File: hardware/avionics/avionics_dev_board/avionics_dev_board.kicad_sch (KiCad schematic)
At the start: 13 parts, among them J1 Screw_Term_1x2, SW1 SW_Push, U1 TPS563200

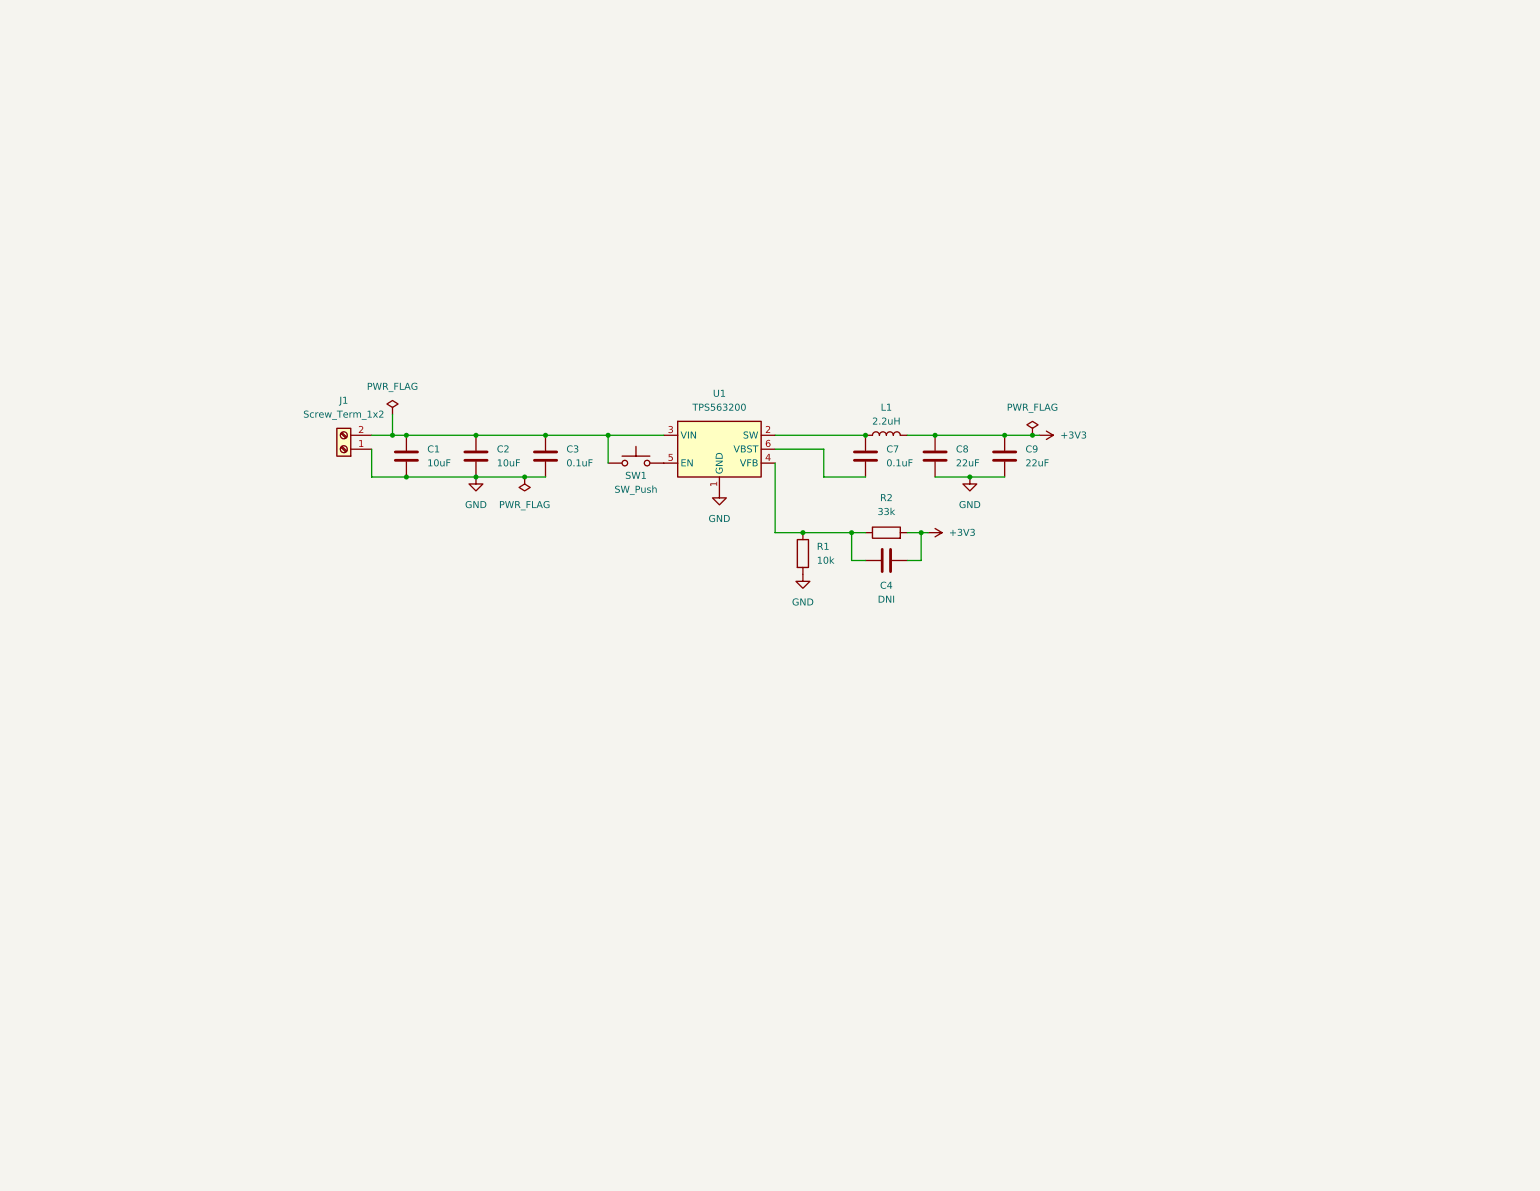
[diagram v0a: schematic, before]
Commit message: Fixed packet sequence miscouting error and finalised avionics component selections
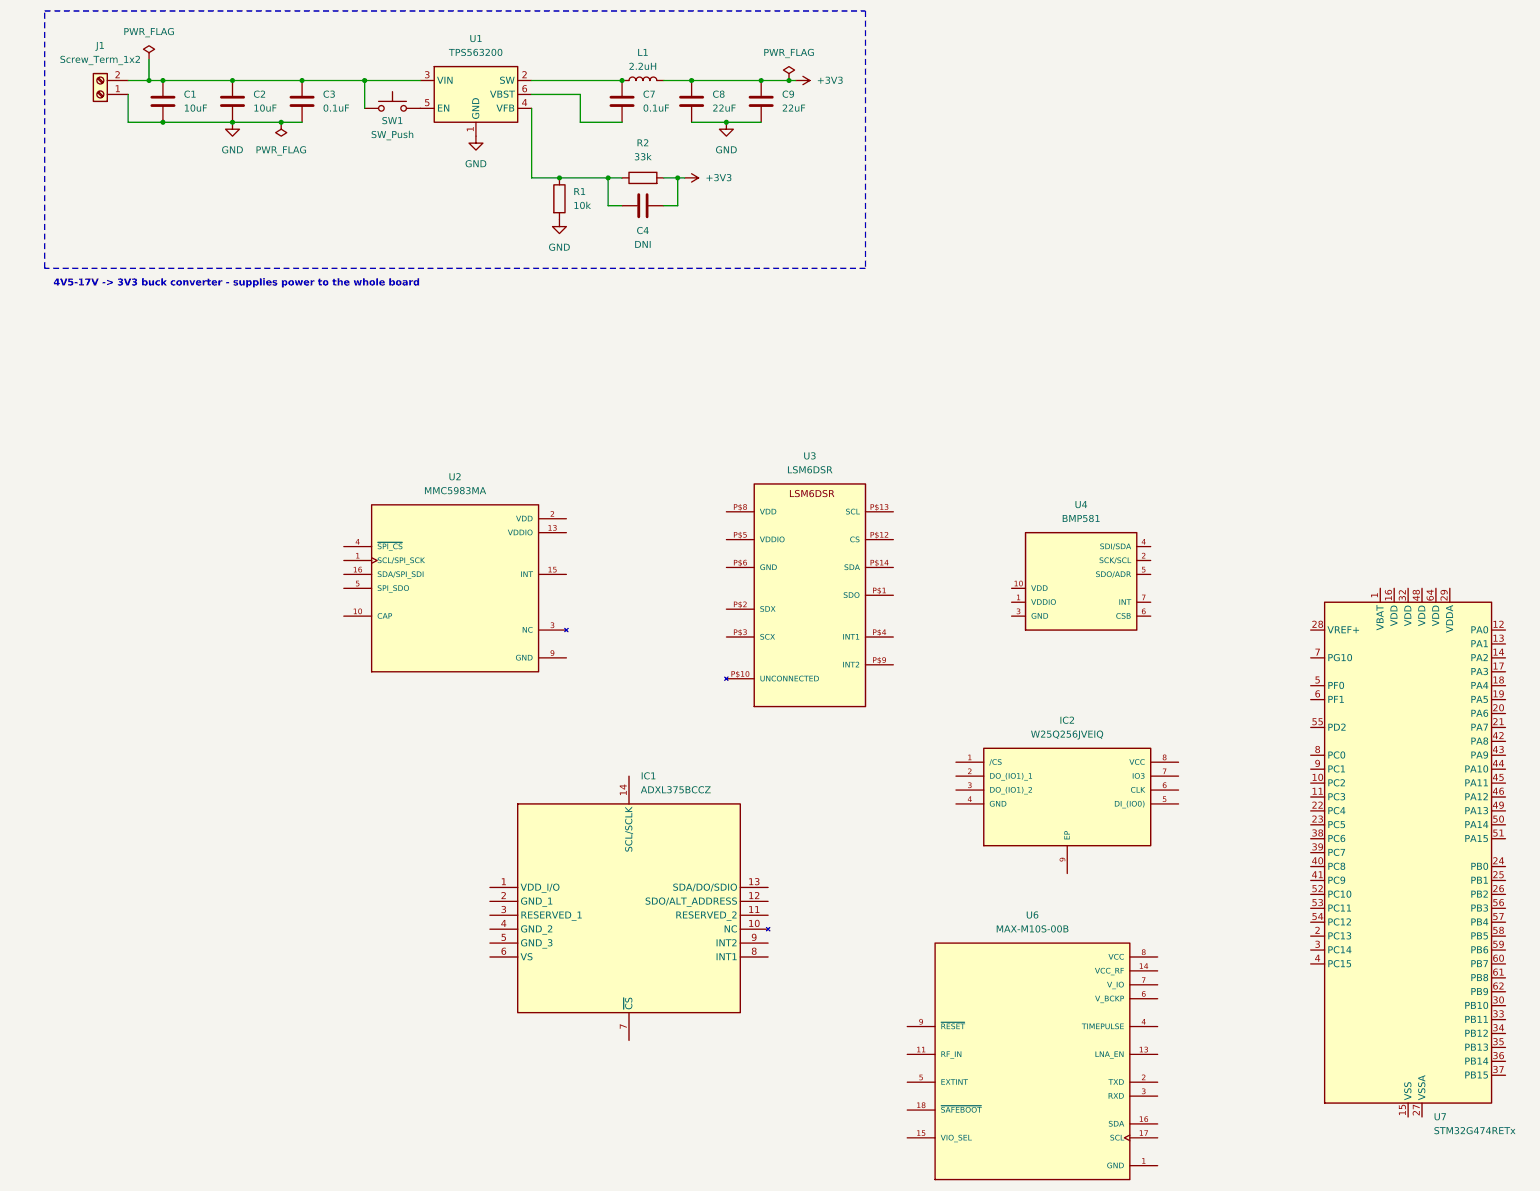
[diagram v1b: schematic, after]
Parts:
- added IC1: ADXL375BCCZ, CC-14-1, symbol ADXL375BCCZ:ADXL375BCCZ
- added IC2: W25Q256JVEIQ, W25Q256JVEIQ:SON127P800X600X80-9N, symbol W25Q256JVEIQ:W25Q256JVEIQ
- added U2: MMC5983MA, MMC5983MA:PQFN50P300X300X100-16N, symbol MMC5983MA:MMC5983MA
- added U3: LSM6DSR, LSM6DSR:LGA-14L, symbol LSM6DSR:LSM6DSR
- added U4: BMP581, BMP581:BMP581, symbol BMP581:BMP581
- added U6: MAX-M10S-00B, MAX-M10S-00B:XCVR_MAX-M10S-00B, symbol MAX-M10S-00B:MAX-M10S-00B
- added U7: STM32G474RETx, Package_QFP:LQFP-64_10x10mm_P0.5mm, symbol MCU_ST_STM32G4:STM32G474RETx
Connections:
- net GND: now also U2.11 (GND), U2.9 (GND), U3.P$6 (GND), U3.P$7 (GND), U4.3 (GND), U4.8 (GND), U4.9 (GND), U6.1 (GND), U6.10 (GND), U6.12 (GND)
- new net: U2.12 (NC), U2.14 (NC), U2.3 (NC), U2.6 (NC), U2.7 (NC), U2.8 (NC)
- new net: U3.P$10 (UNCONNECTED), U3.P$11 (UNCONNECTED)
- new net: U7.15 (VSS), U7.31 (VSS), U7.47 (VSS), U7.63 (VSS)
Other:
- note added: "4V5-17V -> 3V3 buck converter - supplies power to the whole board"
- moved on the sheet: C1, C2, C3, C4, C7, C8, C9, J1, L1, R1, R2, SW1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

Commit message: Started designing stm32g474ret6 section of the PCB schematic. Done power supply, external crystal oscillator, and BOOT0 and NRST pins so far
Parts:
- added C10, C11, C12, C15, C17, C19, C22, C5: 100nF, symbol Device:C
- added C13, C16, C18: 1uF, symbol Device:C
- added C14: 10nF, symbol Device:C
- added C20, C21: ?F, symbol Device:C
- added C6: 4u7F, symbol Device:C
- added D1: PWR LED, symbol Device:LED
- added FB1: 120R, symbol Device:FerriteBead
- added R3: 10k, Resistor_SMD:R_0603_1608Metric, symbol Device:R
- added R4: 10kR, symbol Device:R
- added SW2, SW3: SW_Push, Button_Switch_SMD:SW_DIP_SPSTx01_Slide_6.7x4.1mm_W6.73mm_P2.54mm_LowProfile_JPin, symbol Switch:SW_Push
- added Y1: 32k768Hz, symbol Device:Crystal
- C3, C7: value 0.1uF -> 0u1F
- L1: value 2.2uH -> 2u2H
- U7: value STM32G474RETx -> STM32G474RET6
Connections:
- net +3V3: now also C10.1, C11.1, C12.1, C13.1, C17.1, C5.1, C6.1, FB1.2, R3.1, SW3.2
- net GND: now also U7.1 (VBAT), U7.15 (VSS), U7.16 (VDD), U7.27 (VSSA), U7.31 (VSS), U7.32 (VDD), U7.47 (VSS), U7.48 (VDD), U7.63 (VSS), U7.64 (VDD), C10.2, C11.2, C12.2, C13.2, C14.2, C15.2, C16.2, C17.2, C18.2, C19.2, C20.2, C21.2, C22.2, C5.2, C6.2, D1.1 (K), R4.2, SW2.1
- net +3V3A: now reaches U7.28 (VREF+)
- net +3V3A: now also U7.29 (VDDA), C14.1, C15.1, C16.1, C18.1, FB1.1
- net at U7.5 (PF0): now also C20.1, Y1.1
- net at U7.6 (PF1): now also C21.1, Y1.2
- net at U7.61 (PB8): now also C22.1, R4.1, SW3.1
- net at U7.7 (PG10): now also C19.1, SW2.2
- new net: D1.2 (A), R3.2
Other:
- moved on the sheet: IC1, IC2, U2, U3, U4, U6, U7

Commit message: Updated PCB schematic with sensors and storage devices
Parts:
- added AE1: Antenna, symbol Device:Antenna
- added C23, C24, C25, C27, C28, C31, C32, C33: 100nF, symbol Device:C
- added C26, C30: 1uF, symbol Device:C
- added C29: 10uF, symbol Device:C
- added R10, R5, R6, R7, R8, R9: 2k7R, symbol Device:R
- Y1: value 32k768Hz -> 8MHz
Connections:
- net +3V3: now also IC1.1 (VDD_I/O), IC1.6 (VS), IC2.1 (/CS), IC2.8 (VCC), U2.13 (VDDIO), U2.2 (VDD), U2.4 (~{SPI_CS}), U3.P$5 (VDDIO), U3.P$8 (VDD), U4.1 (VDDIO), U4.10 (VDD), U4.6 (CSB), U6.7 (V_IO), U6.8 (VCC), C23.2, C24.2, C25.2, C26.2, C27.2, C28.2, C30.2, C31.2, C32.2, C33.2, R10.1, R5.2, R6.2, R7.2, R8.2, R9.1
- net GND: now also IC1.2 (GND_1), IC1.4 (GND_2), IC1.5 (GND_3), IC2.4 (GND), IC2.9 (EP), U3.P$2 (SDX), U3.P$3 (SCX), U4.5 (SDO/ADR), C23.1, C24.1, C25.1, C26.1, C27.1, C28.1, C29.1, C30.1, C31.1, C32.1, C33.1
- net BOOT0: now reaches C22.1, R4.1, SW3.1, U7.61 (PB8)
- net I2C2_SCL: now reaches U4.2 (SCK/SCL)
- net I2C2_SCL: now also U2.1 (SCL/SPI_SCK), U6.17 (SCL), U7.43 (PA9), R5.1, R7.1, R9.2
- net I2C2_SDA: now reaches U4.4 (SDI/SDA)
- net I2C2_SDA: now also U2.16 (SDA/SPI_SDI), U6.16 (SDA), U7.42 (PA8), R10.2, R6.1, R8.1
- net INT_BMP: now reaches U4.7 (INT)
- net INT_BMP: now also U7.45 (PA11)
- net NRST: now reaches C19.1, SW2.2, U7.7 (PG10)
- net at U2.10 (CAP): now also C29.2
- net INT_MMC: now reaches U2.15 (INT)
- net INT_MMC: now also U7.44 (PA10)
- net SPI2_MISO: now reaches IC2.2 (DO_(IO1)_1)
- net SPI2_MISO: now also U7.36 (PB14)
- net SPI2_MOSI: now reaches IC2.5 (DI_(IO0))
- net SPI2_MOSI: now also U7.37 (PB15)
- net SPI2_SCK: now reaches IC2.6 (CLK)
- net SPI2_SCK: now also U7.35 (PB13)
- net RST_W25Q: now reaches IC2.7 (IO3)
- net RST_W25Q: now also U7.34 (PB12)
- net SPI1_MISO: now reaches U3.P$1 (SDO)
- net SPI1_MISO: now also IC1.12 (SDO/ALT_ADDRESS), U7.20 (PA6)
- net CS_LSM6: now reaches U3.P$12 (CS)
- net CS_LSM6: now also U7.18 (PA4)
- net SPI1_SCK: now reaches U3.P$13 (SCL)
- net SPI1_SCK: now also IC1.13 (SDA/DO/SDIO), IC1.14 (SCL/SCLK), U7.19 (PA5)
- net SPI1_MOSI: now reaches U3.P$14 (SDA)
- net SPI1_MOSI: now also U7.21 (PA7)
- net LSM6_INT1: now reaches U3.P$4 (INT1)
- net LSM6_INT1: now also U7.22 (PC4)
- net LSM6_INT2: now reaches U3.P$9 (INT2)
- net LSM6_INT2: now also U7.23 (PC5)
- net CS_ADXL: now reaches U7.17 (PA3)
- net CS_ADXL: now also IC1.7 (~{CS})
- net INT1_ADXL: now reaches U7.24 (PB0)
- net INT1_ADXL: now also IC1.8 (INT1)
- net INT2_ADXL: now reaches U7.25 (PB1)
- net INT2_ADXL: now also IC1.9 (INT2)
- net RST_MAX: now reaches U7.46 (PA12)
- net RST_MAX: now also U6.9 (~{RESET})
- net SWDIO: now reaches U7.49 (PA13)
- net SWCLK: now reaches U7.50 (PA14)
- net SPI3_SCK: now reaches U7.52 (PC10)
- net SPI3_MISO: now reaches U7.53 (PC11)
- net SPI3_MOSI: now reaches U7.54 (PC12)
- net at U6.11 (RF_IN): now also AE1.1 (A)
- no-connect marks 0 -> 13
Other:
- note added: "I2C slow sensor block - Barometer, magnetometer, and GPS"
- note added: "SPI1 fast sensor block - Accelerometers"
- note added: "SPI2 storage block"
- moved on the sheet: C22, IC1, IC2, R4, SW3, U2, U3, U4, U6

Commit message: Avionics dev board schematic done
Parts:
- removed R10, R5, R6, R9: 2k7R, symbol Device:R
- added C34, C35, C36: 100nF, symbol Device:C
- added C37: 10nF, symbol Device:C
- added D2: D, symbol Device:D
- added F1: 2A, symbol Device:Fuse
- added J10: Parachute battery, TerminalBlock_Phoenix:TerminalBlock_Phoenix_MKDS-1,5-2-5.08_1x02_P5.08mm_Horizontal, symbol Connector:Screw_Terminal_01x02
- added J2: LAMBDA62, Connector_PinSocket_2.54mm:PinSocket_1x08_P2.54mm_Vertical, symbol Connector:Conn_01x08_Socket
- added J3, J5: Conn_01x08_Socket, Connector_PinSocket_2.54mm:PinSocket_1x08_P2.54mm_Vertical, symbol Connector:Conn_01x08_Socket
- added J4: LAMBDA80, Connector_PinSocket_2.54mm:PinSocket_1x08_P2.54mm_Vertical, symbol Connector:Conn_01x08_Socket
- added J6: SWD interface, symbol Connector_Generic:Conn_02x07_Odd_Even
- added J7: 868MHz antenna, symbol Connector:Conn_Coaxial
- added J8: 2.4GHz antenna, symbol Connector:Conn_Coaxial
- added J9: Nichrome connector, TerminalBlock_Phoenix:TerminalBlock_Phoenix_MKDS-1,5-2-5.08_1x02_P5.08mm_Horizontal, symbol Connector:Screw_Terminal_01x02
- added Q1: Q_NMOS, symbol Device:Q_NMOS
- added R11: 10kR, symbol Device:R
- added R12: 100R, symbol Device:R
- added R13: 0R, symbol Device:R
- added R14, R15: DNI, symbol Device:R
- added SW4: SW_Push, Button_Switch_SMD:SW_DIP_SPSTx01_Slide_6.7x4.1mm_W6.73mm_P2.54mm_LowProfile_JPin, symbol Switch:SW_Push
- AE1: footprint (none) -> avionicsw:Taoglas_CGGP.25.4.A.02
- C3, C7: value 0u1F -> 100nF
- IC1: footprint CC-14-1 -> (none)
- J1: value Screw_Term_1x2 -> Main battery
- R1: value 10k -> 10kR
- R2: value 33k -> 33kR
- R3: value 10k -> 1kR
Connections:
- net +3V3: now also IC2.3 (DO_(IO1)_2), C34.2, C35.2, C36.2, J2.3 (Pin_3), J4.3 (Pin_3), J6.3 (Pin_3); no longer IC2.1 (/CS)
- net GND: now also C34.1, C35.1, C36.1, C37.2, J10.2 (Pin_2), J2.2 (Pin_2), J4.2 (Pin_2), J6.11 (Pin_11), J6.5 (Pin_5), J6.7 (Pin_7), J7.2 (Ext), J8.2 (Ext), Q1.S, R11.2, R14.2, R15.2
- net NRST: now also J6.12 (Pin_12)
- net SPI1_MOSI: now also IC1.13 (SDA/DO/SDIO)
- net SPI1_SCK: no longer IC1.13 (SDA/DO/SDIO)
- net SPI3_MISO: now also J3.6 (Pin_6), J5.6 (Pin_6)
- net SPI3_MOSI: now also J3.7 (Pin_7), J5.7 (Pin_7)
- net SPI3_SCK: now also J3.5 (Pin_5), J5.5 (Pin_5)
- net SWCLK: now also J6.6 (Pin_6)
- net SWDIO: now also J6.4 (Pin_4)
- net at SW1.2: now also C3.2, D2.1 (K); no longer U1.5 (EN)
- net L62_DIO3: now reaches U7.10 (PC2)
- net L62_DIO3: now also J3.1 (Pin_1)
- net L80_DIO3: now reaches U7.11 (PC3)
- net L80_DIO3: now also J5.1 (Pin_1)
- net PARA_DEPLOY: now reaches U7.12 (PA0)
- net PARA_DEPLOY: now also SW4.1
- net L62_RST: now reaches U7.2 (PC13)
- net L62_RST: now also J3.4 (Pin_4)
- net L80_RST: now reaches U7.3 (PC14)
- net L80_RST: now also J5.4 (Pin_4)
- net VCP_RX: now reaches U7.30 (PB10)
- net VCP_RX: now also J6.13 (Pin_13)
- net VCP_TX: now reaches U7.33 (PB11)
- net VCP_TX: now also J6.14 (Pin_14)
- net CS_W25Q: now reaches U7.38 (PC6)
- net CS_W25Q: now also IC2.1 (/CS)
- net L62_DIO2: now reaches U7.4 (PC15)
- net L62_DIO2: now also J2.8 (Pin_8)
- net L62_CS: now reaches U7.51 (PA15)
- net L62_CS: now also J3.8 (Pin_8)
- net L80_CS: now reaches U7.55 (PD2)
- net L80_CS: now also J5.8 (Pin_8)
- net SWO: now reaches U7.56 (PB3)
- net SWO: now also J6.8 (Pin_8)
- net L62_DIO1: now reaches U7.57 (PB4)
- net L62_DIO1: now also J2.7 (Pin_7)
- net L62_BUSY: now reaches U7.58 (PB5)
- net L62_BUSY: now also J2.6 (Pin_6)
- net L80_DIO1: now reaches U7.59 (PB6)
- net L80_DIO1: now also J4.7 (Pin_7)
- net L80_BUSY: now reaches U7.60 (PB7)
- net L80_BUSY: now also J4.6 (Pin_6)
- net L80_DIO2: now reaches U7.62 (PB9)
- net L80_DIO2: now also J4.8 (Pin_8)
- net L62_RXSW: now reaches U7.8 (PC0)
- net L62_RXSW: now also J2.4 (Pin_4)
- net L62_TXSW: now reaches U7.9 (PC1)
- net L62_TXSW: now also J2.5 (Pin_5)
- net at AE1.1 (A): now also R13.1, R14.1; no longer U6.11 (RF_IN)
- new net: J9.1 (Pin_1), Q1.D
- new net: J10.1 (Pin_1), J9.2 (Pin_2)
- new net: C2.2, D2.2 (A), F1.2
- new net: C1.2, F1.1, J1.2 (Pin_2)
- new net: SW1.1, U1.3 (VIN), U1.5 (EN)
- new net: R11.1, R12.1, SW4.2
- new net: C37.1, Q1.G, R12.2
- new net: R13.2, R15.1, U6.11 (RF_IN)
- new net L62_ANT: J2.1 (Pin_1), J7.1 (In)
- new net L80_ANT: J4.1 (Pin_1), J8.1 (In)
- no-connect marks 13 -> 28
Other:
- note added: "4V5-17V -> 3V3 buck converter - supplies power to the whole board Has high current and reverse polarity protection"
- note added: "Microcontroller"
- note added: "Parachute deployment"
- note added: "Pi matching network for tuning if needed"
- note added: "SPI3 LoRa transciever block"
- note added: "Separate battery provides power for melting nichrome wire to prevent brownout of main power source"
- note added: "Serial wire debug interface (programming and debug)"
- note removed: "4V5-17V -> 3V3 buck converter - supplies power to the whole board"
- moved on the sheet: AE1, C1, C10, C11, C12, C13, C14, C15, C16, C17, C18, C19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
